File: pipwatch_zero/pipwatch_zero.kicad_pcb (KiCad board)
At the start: 2 copper layers, 80 x 35 mm, 77 parts, among them P401 CONN_1, P402 CONN_2, P403 CONN_10, Q301 Si1304BDL, Q401 BC849, SW401 TL1014BF180QG, SW402 FSM4JSMATR, SW403 FSM4JSMATR, SW404 FSM4JSMATR, U201 MICRO-B_USB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

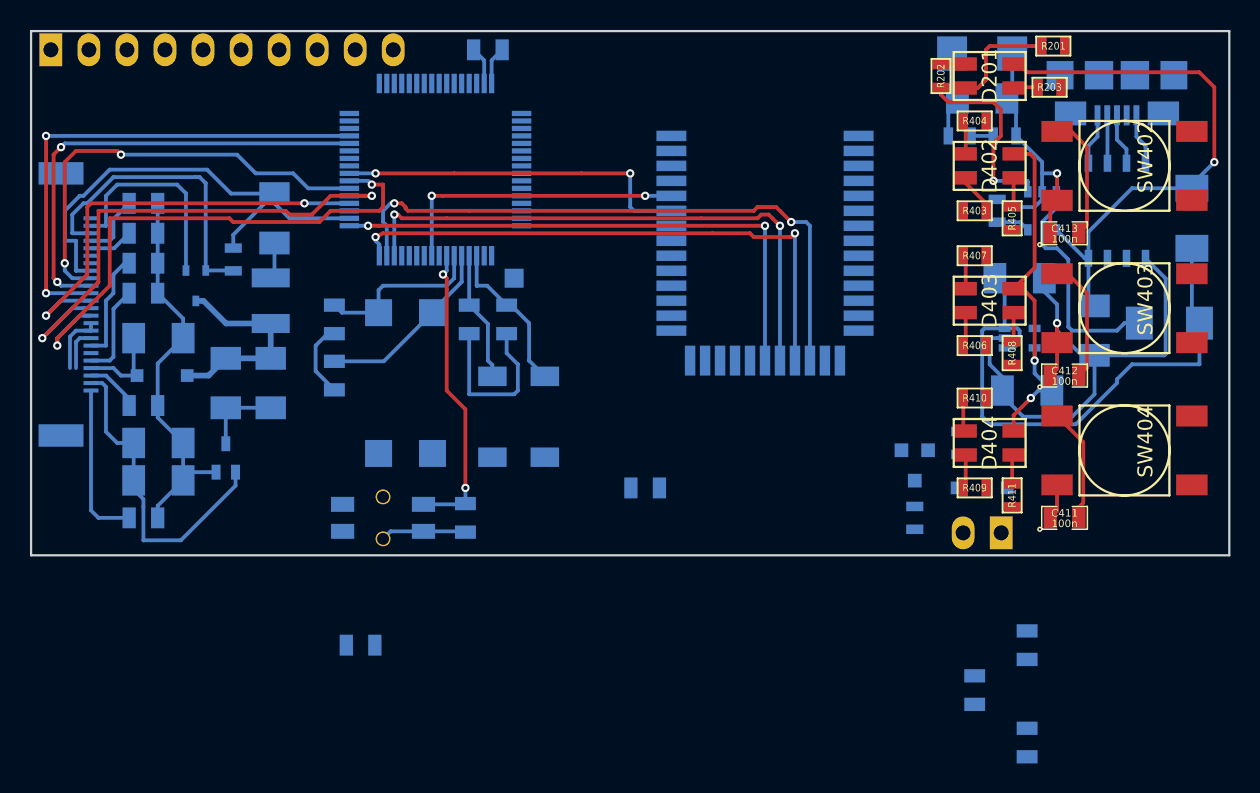
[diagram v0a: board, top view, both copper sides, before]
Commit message: pipwatch_zero layout complete
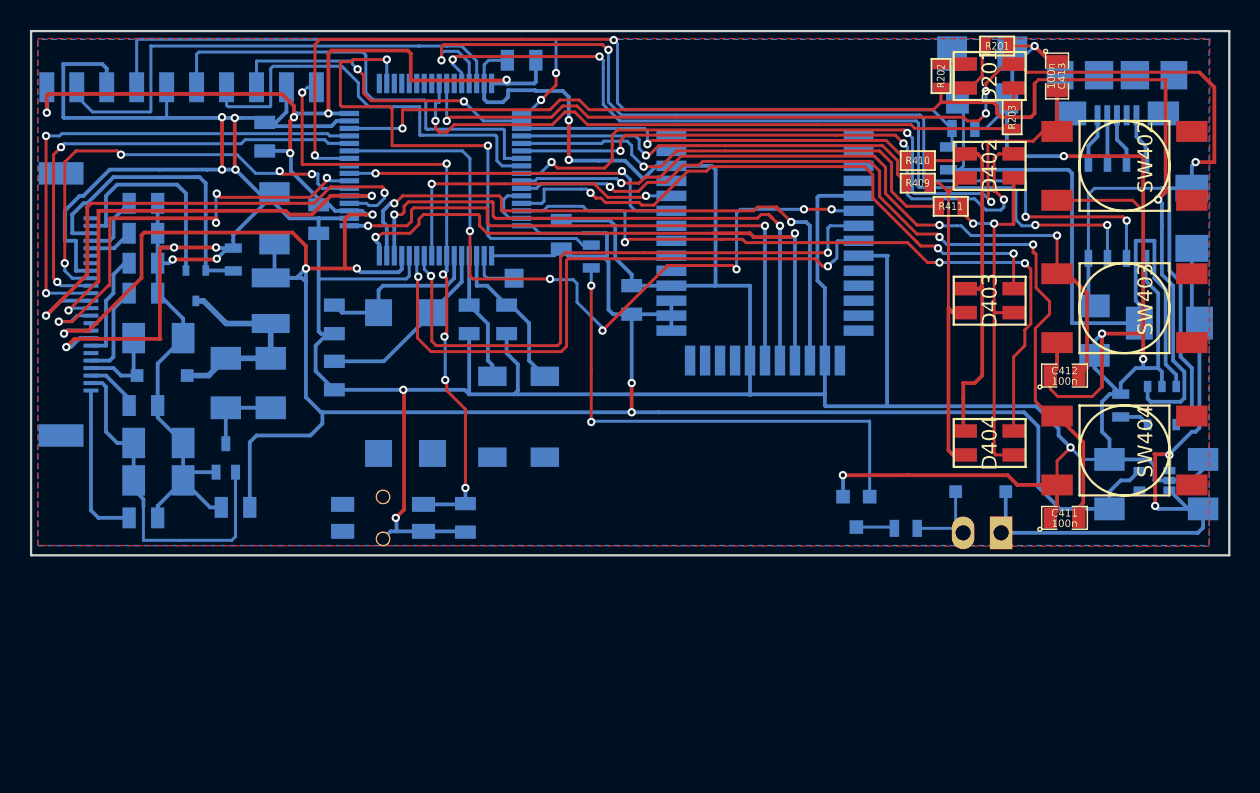
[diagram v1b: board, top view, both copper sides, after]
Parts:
- removed R403, R405, R406, R408: 330, SM0603
- removed R404, R407: 470, SM0603
- P403: footprint pin_strip_10 -> PINARRAY_10P_2MM_SMD
- moved C410 60.1 mm to (137.6, 154.1), turned to 270 degrees
- moved C407 55.1 mm to (135.7, 178.8), turned to 0 degrees
- moved C409 41.4 mm to (157.4, 160.6)
- moved C501 29.3 mm to (162.1, 164.9), turned to 270 degrees
- moved C406 28.2 mm to (141.2, 159.6), turned to 90 degrees
- moved R401 27.6 mm to (159.4, 162.1)
- moved R409 20.7 mm to (181.2, 157.2), turned to 0 degrees
- moved R411 19.7 mm to (183.4, 158.7), turned to 0 degrees
- moved C203 18.4 mm to (200.2, 177.2), turned to 90 degrees
- moved R410 16.3 mm to (181.2, 155.7), turned to 0 degrees
- moved R204 15.4 mm to (194.8, 172.0)
- moved U203 15.3 mm to (197.5, 172.0)
- moved U204 13.1 mm to (197.0, 177.0), turned to 270 degrees
- moved P403 12.0 mm to (123.0, 150.8)
- moved C413 10.5 mm to (190.5, 150.0), turned to 270 degrees
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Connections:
- net N-0000049 renamed /CPU/MOT1P
- net N-0000058 renamed /CPU/LEDBK
- net N-0000062 renamed /CPU/BTN1
- net N-0000063 renamed /CPU/BTN3
- net N-0000068 renamed /CPU/BTN2
- D401 pad 2: 3V3 -> VPP
- D402 pad 1: 3V3 -> /CPU/LED1A
- D402 pad 2: N-0000045 -> N-0000041
- D402 pad 3: N-0000041 -> N-0000042
- D402 pad 4: N-0000044 -> N-0000057
- D403 pad 1: 3V3 -> /CPU/LED2A
- D403 pad 2: N-0000035 -> N-0000041
- D403 pad 3: N-0000038 -> N-0000042
- D403 pad 4: N-0000040 (its old number) -> N-0000057
- D404 pad 1: 3V3 -> /CPU/LED3A
- D404 pad 2: N-0000037 -> N-0000041
- D404 pad 3: N-0000039 (its old number) -> N-0000042
- D404 pad 4: N-0000036 -> N-0000057
- P402 pad 1: 3V3 -> VPP
- R409 pad 1: N-0000060 (its old number) -> /CPU/LEDGK
- R409 pad 2: N-0000036 -> N-0000057
- R410 pad 1: N-0000059 -> /CPU/LEDRK
- R410 pad 2: N-0000039 (its old number) -> N-0000042
- R411 pad 2: N-0000037 -> N-0000041
- U201 pad 4: /Battery and Power/USBID -> (no net)
- U401 pad 35: N-0000043 (its old number) -> (no net)
- U401 pad 36: N-0000056 -> (no net)
- U401 pad 37: N-0000055 -> (no net)
- U401 pad 38: N-0000042 -> (no net)
- U401 pad 39: N-0000061 (its old number) -> (no net)
- U401 pad 40: N-0000057 -> (no net)
- U401 pad 43: /Battery and Power/USBID -> (no net)
- U401 pad 51: N-0000060 (its old number) -> /CPU/LEDRK
- U401 pad 52: N-0000059 -> /CPU/LEDGK
- U401 pad 54: (no net) -> /CPU/LED1A
- U401 pad 61: (no net) -> /CPU/LED2A
- U401 pad 62: (no net) -> /CPU/LED3A
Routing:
- net GND: track 145.8 -> 430.4 mm, vias 2 -> 19
- net 3V3: track 33.3 -> 217.2 mm, vias 2 -> 11
- net /Battery and Power/CHARGESTAT: track 12.9 -> 86.0 mm, vias 1 -> 2
- net /Battery and Power/USBDP: track 0.00 -> 64.2 mm, vias 0 -> 4
- net /Battery and Power/USBPOW: track 37.6 -> 98.0 mm, vias 1 -> 4
- net /Battery and Power/USBDM: track 0.00 -> 57.9 mm, vias 0 -> 4
- net /Battery and Power/VBATSENSE: track 1.48 -> 58.6 mm, vias 0 -> 2
- net /CPU/BTN3: track 7.65 -> 59.5 mm, vias 0 -> 3
- net /BT Modem/BTM_RI: track 0.00 -> 50.4 mm, vias 0 -> 6
- net /CPU/LED3A: track 0.00 -> 48.6 mm, vias 0 -> 3
- net /BT Modem/BTM_DSR: track 0.00 -> 42.9 mm, vias 0 -> 2
- net /Battery and Power/CHARGEBLUE: track 0.00 -> 42.9 mm, vias 0 -> 1
- net /CPU/BTN2: track 8.27 -> 50.9 mm, vias 0 -> 3
- net /BT Modem/BTM_DTR: track 0.00 -> 42.1 mm, vias 0 -> 2
- net /CPU/LED1A: track 0.00 -> 42.0 mm, vias 0 -> 3
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- added copper zone on F.Cu, net 3V3
- added copper zone on B.Cu, net GND
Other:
- net class Default: trace_width 0.254 -> 0.2
- net class Pow2 added: clearance 0.15, trace_width 0.254, via_dia 0.56, via_drill 0.4

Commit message: pipwatch_zero hw02, sent to pragoboard
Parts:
- added 1PIN_S_SMD: P***, 1PIN_S_SMD, B.Cu at (116.0, 67.1)
- added 1PIN_S_SMD: P***, 1PIN_S_SMD, B.Cu at (116.0, 99.8)
- added 1PIN_S_SMD: P***, 1PIN_S_SMD, B.Cu at (193.6, 67.1)
- added 1PIN_S_SMD: P***, 1PIN_S_SMD, B.Cu at (193.4, 99.9)
- added SW405: SW_PUSH, PUSH_SMD_TS1107GS, B.Cu at (153.1, 98.3)
- added SW406: SW_PUSH, PUSH_SMD_TS1107GS, F.Cu at (180.1, 98.7)
- P402: footprint pin_strip_2 -> do214aa
- moved P402 81.6 mm to (178.4, 99.2)
- moved C407 81.3 mm to (128.5, 97.8)
- moved C410 81.3 mm to (130.4, 73.0)
- moved R401 81.3 mm to (152.2, 81.0)
- moved BAT201 81.3 mm to (178.3, 67.5)
- moved C201 81.3 mm to (185.8, 86.0)
- moved C202 81.3 mm to (178.3, 70.5)
- moved C203 81.3 mm to (193.1, 96.2)
- moved C204 81.3 mm to (186.8, 96.2)
- moved C301 81.3 mm to (131.1, 78.5)
- moved C302 81.3 mm to (127.8, 89.5)
- moved C303 81.3 mm to (123.3, 86.5)
- moved C304 81.3 mm to (123.3, 93.5)
- moved C305 81.3 mm to (122.3, 81.5)
- moved C306 81.3 mm to (122.3, 83.5)
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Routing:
- net /CPU/NRST: track 42.5 -> 76.9 mm, vias 6 -> 7
- net GND: track 430.4 -> 447.0 mm
- net /CPU/BTN3: track 59.5 -> 61.9 mm
- net VPP: track 44.3 -> 42.8 mm
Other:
- board text added: "PIP-WATCH"
- board text added: "PIP-WATCH ZERO"
- board text added: "ZERO"
